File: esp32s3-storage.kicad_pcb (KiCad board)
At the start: 2 copper layers, 62.5 x 40.4 mm, 27 parts, among them J1 USB_C_Receptacle_USB2.0_14P, J2 Conn_01x02, J3 Micro_SD_Card, J4 Conn_01x08_Socket, J5 Conn_01x15_Pin, J6 Conn_01x02_Pin, J7 Conn_01x03_Pin, Q1 CJ3401, SW1 SW_Push, SW2 SW_Push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

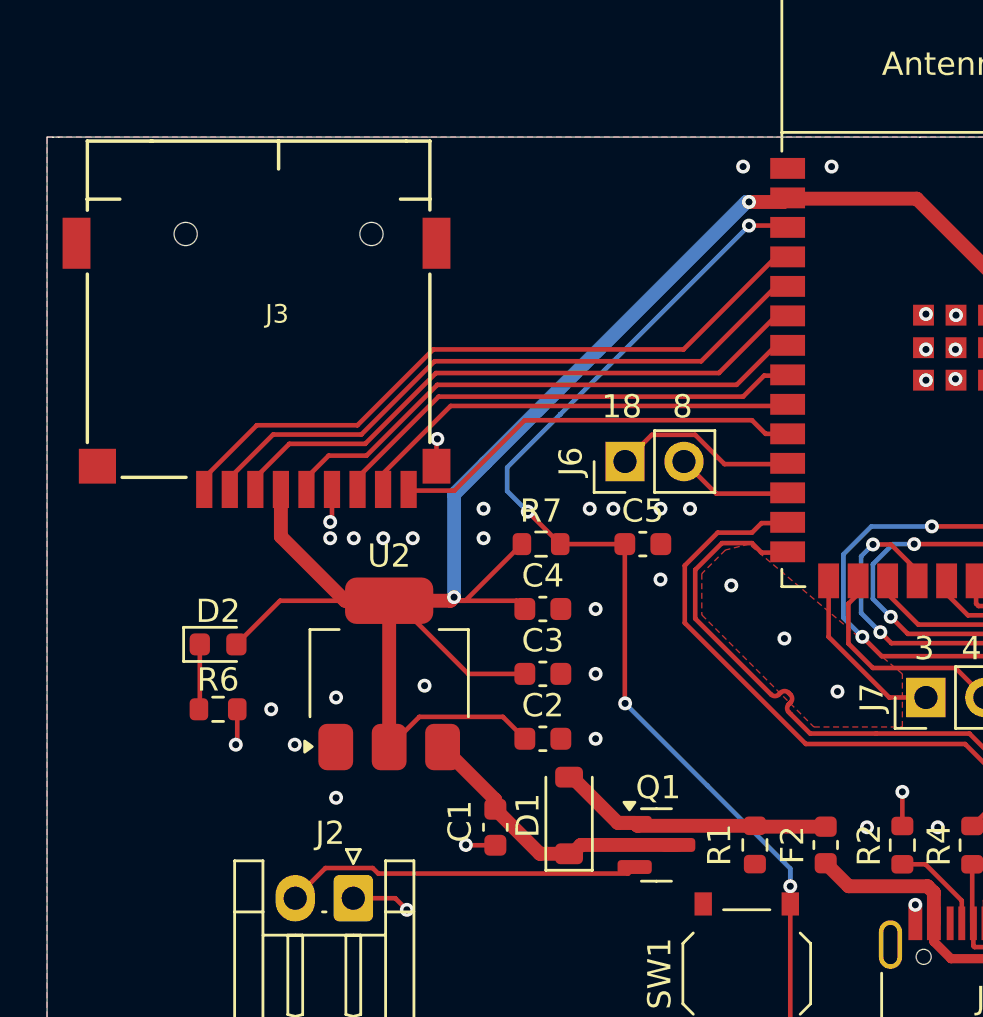
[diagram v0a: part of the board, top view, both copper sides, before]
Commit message: begin modify pcb layout
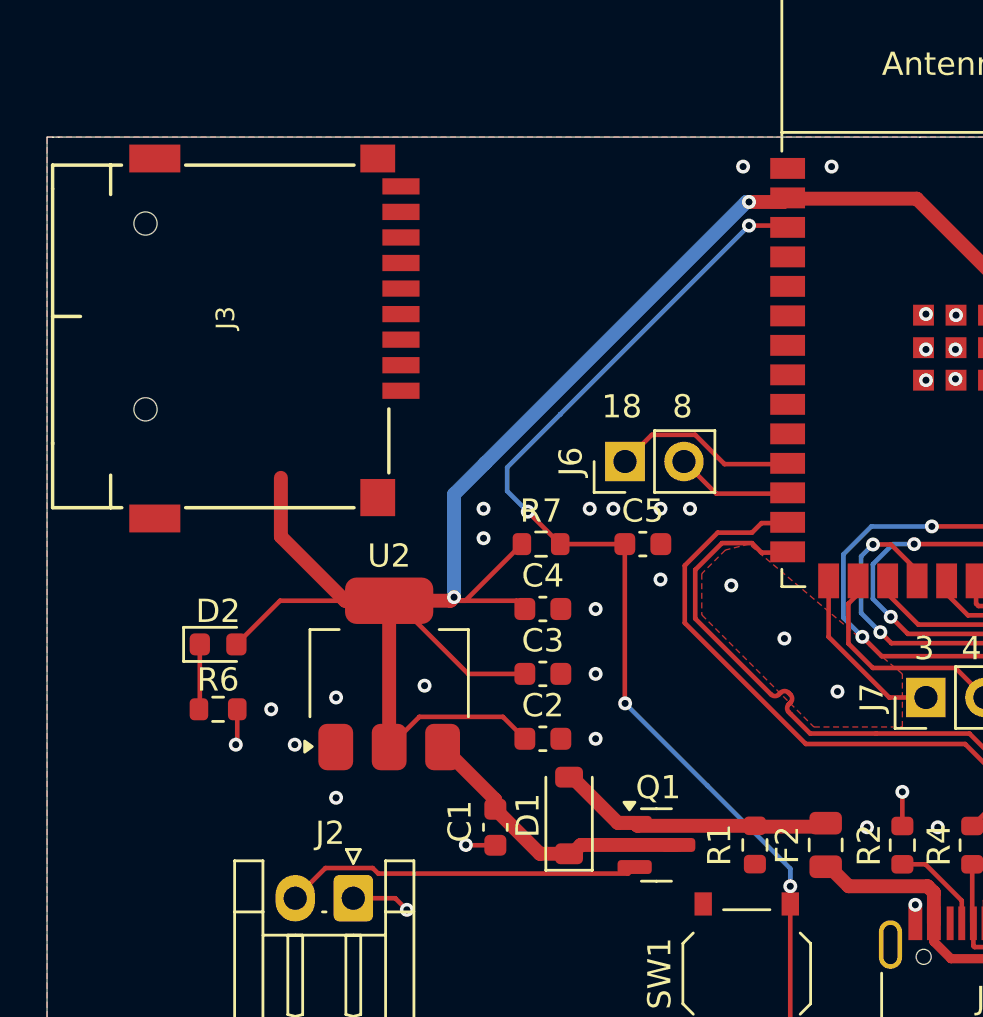
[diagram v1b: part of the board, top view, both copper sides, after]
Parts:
- F2: footprint Fuse:Fuse_0603_1608Metric -> Fuse:Fuse_0805_2012Metric
- moved J3 2.27 mm to (137.8, 105.2), turned to 90 degrees
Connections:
- U1 pad 10: /SDHOST_CDET -> /SDHOST_DAT2
- U1 pad 4: /SDHOST_DAT2 -> /SDHOST_CDET
- U1 pad 5: /SDHOST_DAT3 -> /SDHOST_DAT1
- U1 pad 6: /SDHOST_CMD -> /SDHOST_DAT0
- U1 pad 8: /SDHOST_DAT0 -> /SDHOST_CMD
- U1 pad 9: /SDHOST_DAT1 -> /SDHOST_DAT3
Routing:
- net /SDHOST_DAT2: track 29.0 -> 0.00 mm
- net /SDHOST_DAT3: track 27.4 -> 0.00 mm
- net /SDHOST_CMD: track 25.8 -> 0.00 mm
- net /SDHOST_CLK: track 23.1 -> 0.00 mm
- net /SDHOST_DAT0: track 20.3 -> 0.00 mm
- net /SDHOST_DAT1: track 18.8 -> 0.00 mm
- net /SDHOST_CDET: track 17.8 -> 0.00 mm
- net GND: track 13.5 -> 10.8 mm, vias 48 -> 42

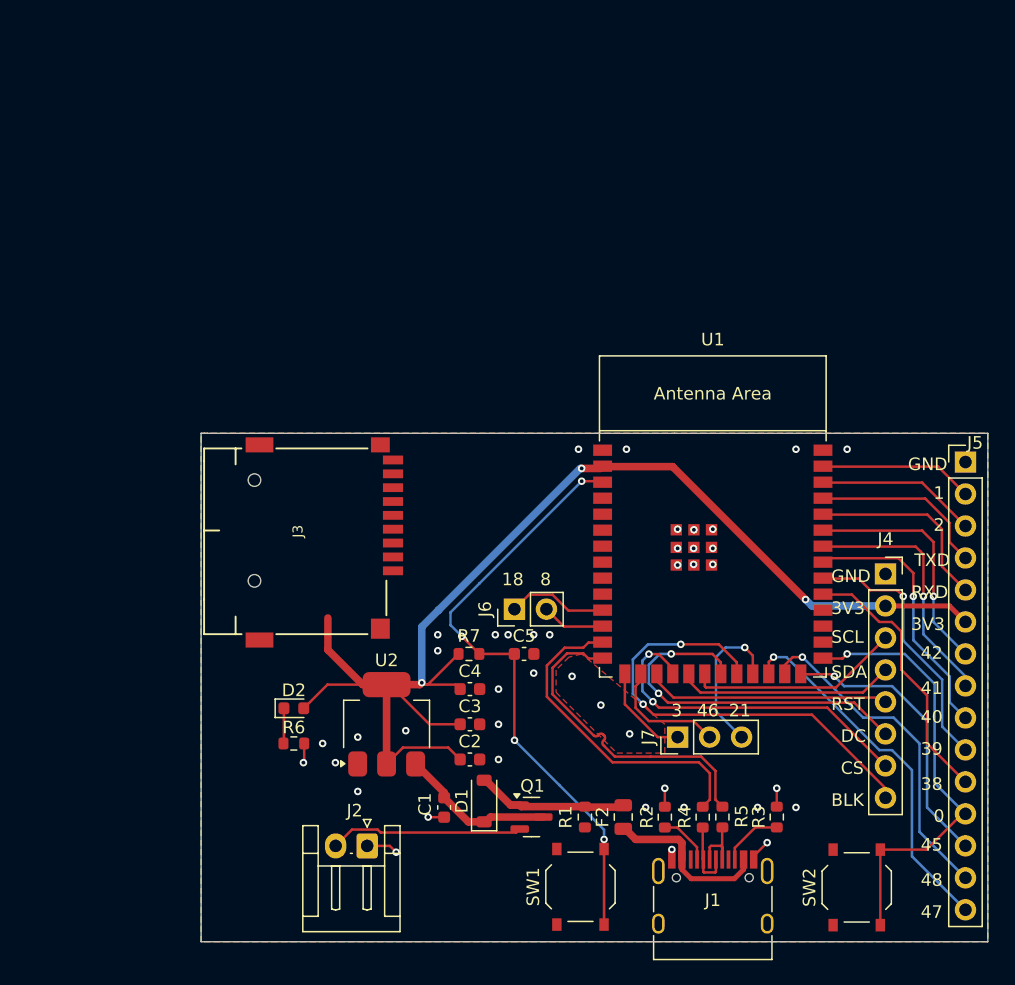
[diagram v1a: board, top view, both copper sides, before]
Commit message: The second version of esp32s3 storage. Becare of the SDIO pins which are changed!
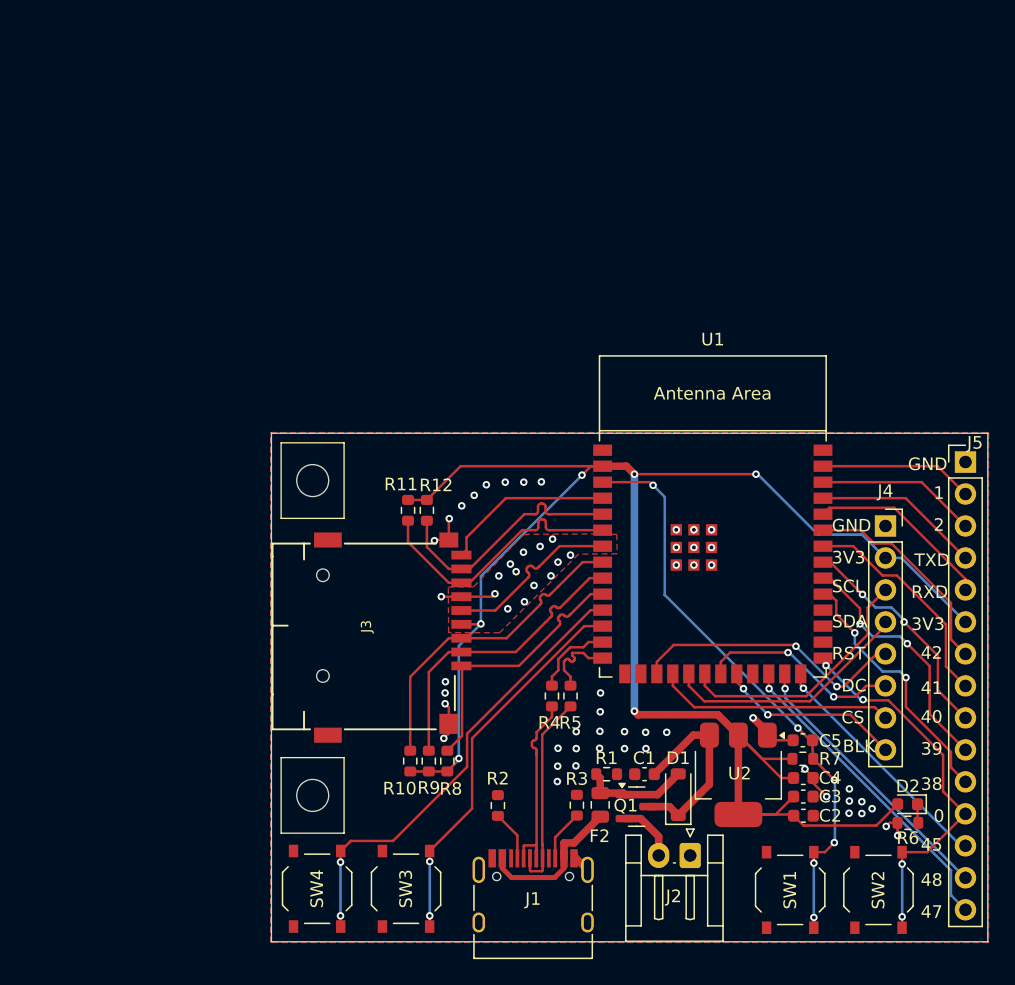
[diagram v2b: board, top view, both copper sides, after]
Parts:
- removed J6: Conn_01x02_Pin, Connector_PinHeader_2.54mm:PinHeader_1x02_P2.54mm_Vertical
- removed J7: Conn_01x03_Pin, Connector_PinHeader_2.54mm:PinHeader_1x03_P2.54mm_Vertical
- added R10: 10K, Resistor_SMD:R_0603_1608Metric, F.Cu at (146.7, 123.6)
- added R11: 10K, Resistor_SMD:R_0603_1608Metric, F.Cu at (146.5, 103.7)
- added R12: 10K, Resistor_SMD:R_0603_1608Metric, F.Cu at (148.0, 103.7)
- added R8: 10K, Resistor_SMD:R_0603_1608Metric, F.Cu at (149.6, 123.6)
- added R9: 10K, Resistor_SMD:R_0603_1608Metric, F.Cu at (148.1, 123.6)
- added SW3: SW_Push, Button_Switch_SMD:SW_Push_1P1T_XKB_TS-1187A, F.Cu at (146.3, 133.7)
- added SW4: SW_Push, Button_Switch_SMD:SW_Push_1P1T_XKB_TS-1187A, F.Cu at (139.3, 133.7)
- moved D2 49.3 mm to (186.2, 127.0), turned to 180 degrees
- moved R6 49.2 mm to (186.2, 128.5), turned to 180 degrees
- moved U2 28.2 mm to (172.7, 124.7), turned to -90 degrees
- moved R7 27.8 mm to (177.8, 123.4)
- moved C4 27.4 mm to (177.9, 124.9)
- moved C3 27.1 mm to (177.9, 126.4)
- moved C2 26.9 mm to (177.9, 127.9)
- moved J2 25.7 mm to (168.9, 131.1)
- moved C5 23.2 mm to (177.8, 121.9), turned to 180 degrees
- moved SW1 16.7 mm to (176.8, 133.8)
- moved C1 16.1 mm to (165.3, 124.6), turned to 180 degrees
- moved R3 15.9 mm to (159.9, 127.1)
- moved R5 15.4 mm to (159.4, 118.4)
- moved D1 15.4 mm to (167.9, 126.2)
- moved R4 15.4 mm to (157.9, 118.4)
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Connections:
- U1 pad 15: /GPIO3 -> unconnected-(U1-IO3-Pad15)
- U1 pad 16: /GPIO46 -> unconnected-(U1-IO46-Pad16)
- U1 pad 23: /GPIO21 -> unconnected-(U1-IO21-Pad23)
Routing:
- net /3V3: track 109.5 -> 148.6 mm, vias 3 -> 6
- net /GPIO18: track 8.00 -> 36.3 mm, vias 0 -> 2
- net /SDHOST_CMD: track 0.00 -> 25.4 mm
- net /GPIO8: track 5.03 -> 30.4 mm, vias 0 -> 2
- net /SDHOST_DAT3: track 0.00 -> 23.7 mm
- net /LCD_BLK: track 37.0 -> 14.8 mm
- net /SDHOST_DAT0: track 0.00 -> 21.5 mm
- net /SDHOST_DAT2: track 0.00 -> 21.4 mm
- net /SDHOST_DAT1: track 0.00 -> 19.8 mm
- net /ESP32S3_USB_N: track 26.0 -> 6.39 mm
- net /ESP32S3_USB_P: track 26.0 -> 6.36 mm
- net /SDHOST_CLK: track 0.00 -> 14.1 mm
- net /SDHOST_CDET: track 0.00 -> 13.7 mm
- net /LCD_DC: track 29.2 -> 16.2 mm
- net /GPIO21: track 12.2 -> 0.00 mm, vias 1 -> 0
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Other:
- board size 62.5 x 40.4 mm -> 56.9 x 40.4 mm
- board text removed: "18"
- board text removed: "21"
- board text removed: "3"
- board text removed: "46"
- board text removed: "8"

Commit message: add silk to switches
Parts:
- moved SW3 1.02 mm to (147.3, 133.7)
- moved SW4 1.02 mm to (140.3, 133.7)
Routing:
- net /GPIO18: track 36.3 -> 35.3 mm
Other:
- board text added: "Boot"
- board text added: "IO18"
- board text added: "IO8"
- board text added: "Reset"
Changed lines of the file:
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@@
 	(footprint "Button_Switch_SMD:SW_Push_1P1T_XKB_TS-1187A"
 		(layer "F.Cu")
-		(at 146.3258 133.7136 90)
+		(at 147.3418 133.7136 90)
 		(descr "SMD Tactile Switch, http://www.helloxkb.com/public/images/pdf/TS-1187A-X-X-X.pdf")
 		(tags "SPST Tactile Switch")
@@
 	(footprint "Button_Switch_SMD:SW_Push_1P1T_XKB_TS-1187A"
 		(layer "F.Cu")
-		(at 139.2646 133.7136 90)
+		(at 140.2806 133.7136 90)
 		(descr "SMD Tactile Switch, http://www.helloxkb.com/public/images/pdf/TS-1187A-X-X-X.pdf")
 		(tags "SPST Tactile Switch")
@@
 		)
 	)
+	(gr_text "IO8"
+		(at 144.4244 135.8392 90)
+		(layer "F.SilkS")
+		(effects
+			(font
+				(size 1 1)
+				(thickness 0.1)
+			)
+			(justify left bottom)
+		)
+	)
 	(gr_text "1"
 		(at 188.214 102.87 0)
@@
 		)
 	)
+	(gr_text "IO18"
+		(at 137.3124 135.8392 90)
+		(layer "F.SilkS")
+		(effects
+			(font
+				(size 1 1)
+				(thickness 0.1)
+			)
+			(justify left bottom)
+		)
+	)
 	(gr_text "0"
 		(at 188.214 128.524 0)
@@
 		)
 	)
+	(gr_text "Boot"
+		(at 180.9242 135.8392 90)
+		(layer "F.SilkS")
+		(effects
+			(font
+				(size 1 1)
+				(thickness 0.1)
+			)
+			(justify left bottom)
+		)
+	)
 	(gr_text "41"
 		(at 187.198 118.364 0)
@@
 		)
 	)
+	(gr_text "Reset"
+		(at 173.9138 135.8392 90)
+		(layer "F.SilkS")
+		(effects
+			(font
+				(size 1 1)
+				(thickness 0.1)
+			)
+			(justify left bottom)
+		)
+	)
 	(gr_text "GND"
 		(at 180.1368 105.4608 0)
@@
 	)
 	(segment
-		(start 151.5736 121.760914)
-		(end 151.5736 127.3408)
+		(start 151.5736 128.3568)
+		(end 149.2168 130.7136)
 		(width 0.2)
 		(layer "F.Cu")
@@
 	)
 	(segment
-		(start 148.209 136.7054)
-		(end 148.2008 136.7136)
+		(start 149.225 136.7054)
+		(end 149.2168 136.7136)
 		(width 0.2)
 		(layer "F.Cu")
@@
 	)
 	(segment
-		(start 148.2008 131.5384)
-		(end 148.209 131.5466)
+		(start 149.2168 131.5384)
+		(end 149.225 131.5466)
 		(width 0.2)
 		(layer "F.Cu")
@@
 	)
 	(segment
-		(start 148.209 135.8646)
-		(end 148.209 136.7054)
+		(start 151.5736 121.760914)
+		(end 151.5736 128.3568)
 		(width 0.2)
 		(layer "F.Cu")
@@
 	)
 	(segment
-		(start 148.2008 130.7136)
-		(end 148.2008 131.5384)
+		(start 149.225 135.8646)
+		(end 149.225 136.7054)
 		(width 0.2)
 		(layer "F.Cu")
@@
 	)
 	(segment
-		(start 151.5736 127.3408)
-		(end 148.2008 130.7136)
+		(start 149.2168 130.7136)
+		(end 149.2168 131.5384)
 		(width 0.2)
 		(layer "F.Cu")
@@
 	)
 	(via
-		(at 148.209 135.8646)
+		(at 149.225 135.8646)
 		(size 0.6)
 		(drill 0.3)
@@
 	)
 	(via
-		(at 148.209 131.5466)
+		(at 149.225 131.5466)
 		(size 0.6)
 		(drill 0.3)
@@
 	)
 	(segment
-		(start 148.209 131.5466)
-		(end 148.209 135.8646)
+		(start 149.225 131.5466)
+		(end 149.225 135.8646)
 		(width 0.2)
 		(layer "B.Cu")
@@
 	)
 	(segment
-		(start 141.1396 131.5802)
-		(end 141.1224 131.5974)
+		(start 142.1556 131.5802)
+		(end 142.1384 131.5974)
 		(width 0.2)
 		(layer "F.Cu")
@@
 	)
 	(segment
-		(start 141.1224 136.6964)
-		(end 141.1396 136.7136)
+		(start 142.1384 136.6964)
+		(end 142.1556 136.7136)
 		(width 0.2)
 		(layer "F.Cu")
@@
 	)
 	(segment
-		(start 145.2954 129.9136)
-		(end 141.9396 129.9136)
+		(start 142.9556 129.9136)
+		(end 142.1556 130.7136)
 		(width 0.2)
 		(layer "F.Cu")
@@
 	)
 	(segment
-		(start 141.1396 130.7136)
-		(end 141.1396 131.5802)
+		(start 145.276048 129.9136)
+		(end 142.9556 129.9136)
 		(width 0.2)
 		(layer "F.Cu")
@@
 	)
 	(segment
-		(start 141.1224 135.8646)
-		(end 141.1224 136.6964)
+		(start 142.1556 130.7136)
+		(end 142.1556 131.5802)
 		(width 0.2)
 		(layer "F.Cu")
@@
 	)
 	(segment
-		(start 151.1736 121.3984)
-		(end 151.1736 124.0354)
+		(start 142.1384 135.8646)
+		(end 142.1384 136.6964)
 		(width 0.2)
 		(layer "F.Cu")
@@
 	)
 	(segment
-		(start 160.988 111.584)
-		(end 151.1736 121.3984)
+		(start 151.1736 124.016048)
+		(end 145.276048 129.9136)
 		(width 0.2)
 		(layer "F.Cu")
@@
 	)
 	(segment
-		(start 141.9396 129.9136)
-		(end 141.1396 130.7136)
+		(start 160.988 111.584)
+		(end 151.1736 121.3984)
 		(width 0.2)
 		(layer "F.Cu")
@@
 	)
 	(segment
-		(start 151.1736 124.0354)
-		(end 145.2954 129.9136)
+		(start 151.1736 121.3984)
+		(end 151.1736 124.016048)
 		(width 0.2)
 		(layer "F.Cu")
@@
 	)
 	(via
-		(at 141.1224 135.8646)
+		(at 142.1384 135.8646)
 		(size 0.6)
 		(drill 0.3)
@@
 	)
 	(via
-		(at 141.1224 131.5974)
+		(at 142.1384 131.5974)
 		(size 0.6)
 		(drill 0.3)
@@
 	)
 	(segment
-		(start 141.1224 131.5974)
-		(end 141.1224 135.8646)
+		(start 142.1384 131.5974)
+		(end 142.1384 135.8646)
 		(width 0.2)
 		(layer "B.Cu")

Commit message: esp32s3-storage v3
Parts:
- removed J5: Conn_01x15_Pin, Connector_PinHeader_2.54mm:PinHeader_1x15_P2.54mm_Vertical
- added C6: 0.1uF, Capacitor_SMD:C_0603_1608Metric, F.Cu at (148.5, 80.6)
- added J6: ~, user_created:fpc connector 1x12 P0.5mm bottom-side back-flip, F.Cu at (148.8, 89.9)
- added Q2: SS8050, Package_TO_SOT_SMD:SOT-23, F.Cu at (157.2, 84.5)
- added R13: 10R, Resistor_SMD:R_0603_1608Metric, F.Cu at (153.7, 85.1)
- added R14: 1K, Resistor_SMD:R_0603_1608Metric, F.Cu at (153.7, 86.6)
- added R15: 10K, Resistor_SMD:R_0603_1608Metric, F.Cu at (153.7, 83.6)
- D2, R6: moved to B.Cu
- J2: footprint Connector_JST:JST_EH_S2B-EH_1x02_P2.50mm_Horizontal -> Connector_JST:JST_GH_SM02B-GHS-TB_1x02-1MP_P1.25mm_Horizontal
- J4: value Conn_01x08_Socket -> Conn_01x03_Pin; footprint Connector_PinSocket_2.54mm:PinSocket_1x08_P2.54mm_Vertical -> Connector_PinHeader_2.54mm:PinHeader_1x03_P2.54mm_Vertical
- SW1, SW2, SW3, SW4: footprint Button_Switch_SMD:SW_Push_1P1T_XKB_TS-1187A -> Button_Switch_SMD:SW_SPST_PTS647_Sx38; moved to B.Cu
- moved R6 67.7 mm to (153.5, 69.2)
- moved J1 67.5 mm to (143.8, 69.1), turned to 180 degrees
- moved D2 64.9 mm to (153.5, 70.9)
- moved J2 63.1 mm to (153.7, 69.8)
- moved J4 55.3 mm to (131.1, 119.6), turned to -90 degrees
- moved Q1 54.4 mm to (158.9, 73.1), turned to 90 degrees
- moved R3 54.3 mm to (141.5, 75.9), turned to -90 degrees
- moved D1 54.2 mm to (152.7, 74.3), turned to 180 degrees
- moved F2 52.3 mm to (148.6, 76.5), turned to 0 degrees
- moved R2 51.9 mm to (145.0, 75.9), turned to -90 degrees
- moved R7 50.7 mm to (148.5, 82.1), turned to 180 degrees
- moved C2 50.2 mm to (160.7, 80.8)
- moved C3 50.2 mm to (160.6, 79.2)
- moved C4 50.2 mm to (160.6, 77.8)
- moved U2 49.0 mm to (154.7, 79.1), turned to 180 degrees
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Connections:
- J4 pad 2: /3V3 -> /TXD0
- J4 pad 3: /LCD_SCL -> /RXD0
- U1 pad 15: unconnected-(U1-IO3-Pad15) -> /GPIO3_S
- U1 pad 16: unconnected-(U1-IO46-Pad16) -> /GPIO46_S
- U1 pad 23: unconnected-(U1-IO21-Pad23) -> /GPIO21
- U1 pad 26: /GPIO45 -> /GPIO45_S
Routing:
- net /3V3: track 148.6 -> 116.9 mm, vias 6 -> 3
- net /GPIO47: track 25.2 -> 0.00 mm, vias 1 -> 0
- net /GPIO48: track 22.1 -> 0.00 mm, vias 1 -> 0
- net /TXD0: track 13.3 -> 34.9 mm
- net /GPIO38: track 20.7 -> 0.00 mm, vias 2 -> 0
- net /GPIO39: track 19.9 -> 0.00 mm, vias 2 -> 0
- net /GPIO45: track 19.3 -> 0.00 mm, vias 1 -> 0
- net /LCD_BLK: track 14.8 -> 33.5 mm
- net /GPIO40: track 18.1 -> 0.00 mm, vias 2 -> 0
- net /GPIO41: track 17.9 -> 0.00 mm
- net /GPIO42: track 17.1 -> 0.00 mm
- net /GPIO18: track 35.3 -> 18.6 mm, vias 2 -> 1
- net /SDHOST_DAT0: track 21.5 -> 37.8 mm
- net /BOOT: track 30.6 -> 15.1 mm, vias 4 -> 1
- net /SDHOST_DAT1: track 19.8 -> 35.1 mm
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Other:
- board size 56.9 x 40.4 mm -> 47.6 x 55.8 mm
- board text removed: "0"
- board text removed: "1"
- board text removed: "2"
- board text removed: "38"
- board text removed: "39"
- board text removed: "3V3"
- board text removed: "40"
- board text removed: "41"
- board text removed: "42"
- board text removed: "45"
- board text removed: "47"
- board text removed: "48"
- board text removed: "BLK"
- board text removed: "Boot"
- board text removed: "CS"
- board text removed: "DC"
- board text removed: "GND"
- board text removed: "IO18"
- board text removed: "IO8"
- board text removed: "RST"
- board text removed: "RXD"
- board text removed: "Reset"
- board text removed: "SCL"
- board text removed: "SDA"
- board text removed: "TXD"

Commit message: esp32s3-storage v4
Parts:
- moved J6 4.00 mm to (144.8, 89.9)
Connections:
- J6 pad 13: (no net) -> GND
- J6 pad 14: (no net) -> GND
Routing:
- net /3V3: track 116.9 -> 134.8 mm
- net GND: track 18.2 -> 26.9 mm, vias 33 -> 93
- net /LCD_LEDK: track 4.06 -> 10.2 mm
- net /SDHOST_CDET: track 28.2 -> 32.4 mm, vias 0 -> 2
- net /LCD_DC: track 30.4 -> 26.3 mm
- net /LCD_RST: track 23.0 -> 24.7 mm
- net /SDHOST_DAT0: track 37.8 -> 39.4 mm
- net /SDHOST_DAT2: track 31.9 -> 33.4 mm
- net /SDHOST_DAT1: track 35.1 -> 36.6 mm
- net /SDHOST_DAT3: track 35.8 -> 37.3 mm
- net /SDHOST_CMD: track 38.3 -> 39.7 mm
- net /SDHOST_CLK: track 28.9 -> 30.4 mm
- net /LCD_SCL: track 27.7 -> 26.5 mm
- net /LCD_BLK: track 33.5 -> 34.3 mm
- net /LCD_SDA: track 25.6 -> 26.3 mm
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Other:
- board size 47.6 x 55.8 mm -> 47.5 x 55.8 mm
- board text added: "Boot"
- board text added: "IO18"
- board text added: "IO8"
- board text added: "Reset"

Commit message: esp32s3-storage v5
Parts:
- J2: footprint Connector_JST:JST_GH_SM02B-GHS-TB_1x02-1MP_P1.25mm_Horizontal -> user_created:1x2 pin gap 1.25mm SMD socket
- J6: footprint user_created:fpc connector 1x12 P0.5mm bottom-side back-flip -> user_created:JST AFC01-S12FCC-00 1x2 P0.5mm back-flip bottom-side
- moved J6 1.80 mm to (146.6, 89.9)
- moved J2 1.60 mm to (154.3, 68.4)
- moved Q2 0.29 mm to (157.2, 84.7)
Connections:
- J2 pad 1: GND -> /VBAT
- J2 pad 2: /VBAT -> GND
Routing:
- net /3V3: track 134.8 -> 121.0 mm
- net GND: track 26.9 -> 38.9 mm, vias 93 -> 144
- net /VBAT: track 10.9 -> 7.83 mm
- net /GPIO18: track 18.6 -> 21.2 mm
- net /LCD_CS: track 24.1 -> 26.6 mm
- net /LCD_RST: track 24.7 -> 26.6 mm
- net /LCD_SDA: track 26.3 -> 28.0 mm
- net /LCD_SCL: track 26.5 -> 28.2 mm
- net /LCD_DC: track 26.3 -> 28.1 mm
- net /CHIP_UP: track 39.2 -> 38.3 mm
